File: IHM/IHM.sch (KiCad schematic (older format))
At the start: 29 parts, among them J1 JACK, SW1 BTN_R1, SW2 BTN_L1, SW3 BTN_L2, SW4 BTN_R2, U1 WeMos_D1_mini

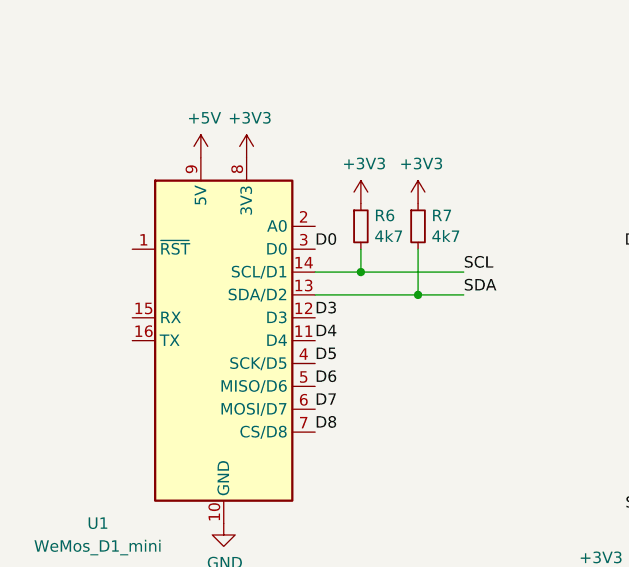
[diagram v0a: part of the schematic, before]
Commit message: Add LCSC references
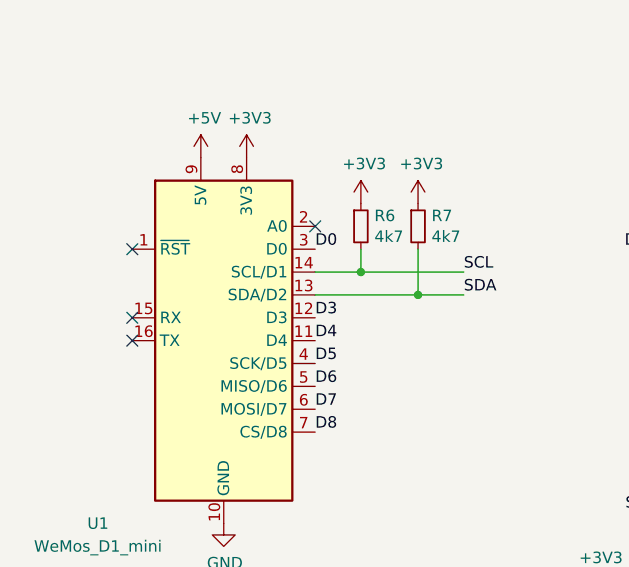
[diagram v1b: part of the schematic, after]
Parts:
- C1, C2, C3, C4, C5: LCSC (none) -> C14663
- R1, R2, R3, R4, R5: LCSC (none) -> C25804
- R6, R7: LCSC (none) -> C23162
- RG1, RR1: LCSC (none) -> C22843
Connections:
- no-connect marks 0 -> 4
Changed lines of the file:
@@
 F 2 "Resistor_SMD:R_0603_1608Metric" V 5280 3000 50  0001 C CNN
 F 3 "~" H 5350 3000 50  0001 C CNN
+F 4 "C25804" H 5350 3000 50  0001 C CNN "LCSC"
 	1    5350 3000
 	-1   0    0    1
@@
 F 2 "Resistor_SMD:R_0603_1608Metric" V 5230 1100 50  0001 C CNN
 F 3 "~" H 5300 1100 50  0001 C CNN
+F 4 "C22843" H 5300 1100 50  0001 C CNN "LCSC"
 	1    5300 1100
 	0    1    1    0
@@
 F 2 "Resistor_SMD:R_0603_1608Metric" V 5230 1600 50  0001 C CNN
 F 3 "~" H 5300 1600 50  0001 C CNN
+F 4 "C22843" H 5300 1600 50  0001 C CNN "LCSC"
 	1    5300 1600
 	0    1    1    0
@@
 F 2 "Resistor_SMD:R_0603_1608Metric" V 6230 3000 50  0001 C CNN
 F 3 "~" H 6300 3000 50  0001 C CNN
+F 4 "C25804" H 6300 3000 50  0001 C CNN "LCSC"
 	1    6300 3000
 	-1   0    0    1
@@
 F 2 "Resistor_SMD:R_0603_1608Metric" V 7180 3000 50  0001 C CNN
 F 3 "~" H 7250 3000 50  0001 C CNN
+F 4 "C25804" H 7250 3000 50  0001 C CNN "LCSC"
 	1    7250 3000
 	-1   0    0    1
@@
 F 2 "Resistor_SMD:R_0603_1608Metric" V 7330 1650 50  0001 C CNN
 F 3 "~" H 7400 1650 50  0001 C CNN
+F 4 "C25804" H 7400 1650 50  0001 C CNN "LCSC"
 	1    7400 1650
 	-1   0    0    1
@@
 F 2 "Resistor_SMD:R_0603_1608Metric" H 3900 3050 50  0001 C CNN
 F 3 "~" H 3900 3050 50  0001 C CNN
+F 4 "C23162" H 3900 3050 50  0001 C CNN "LCSC"
 	1    3900 3050
 	1    0    0    -1
@@
 F 2 "Resistor_SMD:R_0603_1608Metric" H 4150 3050 50  0001 C CNN
 F 3 "~" H 4150 3050 50  0001 C CNN
+F 4 "C23162" H 4150 3050 50  0001 C CNN "LCSC"
 	1    4150 3050
 	1    0    0    -1
@@
 F 2 "Capacitor_SMD:C_0603_1608Metric" H 5888 3200 50  0001 C CNN
 F 3 "~" H 5850 3350 50  0001 C CNN
+F 4 "C14663" H 5850 3350 50  0001 C CNN "LCSC"
 	1    5850 3350
 	1    0    0    -1
@@
 F 2 "Capacitor_SMD:C_0603_1608Metric" H 6838 3200 50  0001 C CNN
 F 3 "~" H 6800 3350 50  0001 C CNN
+F 4 "C14663" H 6800 3350 50  0001 C CNN "LCSC"
 	1    6800 3350
 	1    0    0    -1
@@
 F 2 "Capacitor_SMD:C_0603_1608Metric" H 7788 3200 50  0001 C CNN
 F 3 "~" H 7750 3350 50  0001 C CNN
+F 4 "C14663" H 7750 3350 50  0001 C CNN "LCSC"
 	1    7750 3350
 	1    0    0    -1
@@
 F 2 "Capacitor_SMD:C_0603_1608Metric" H 7038 1800 50  0001 C CNN
 F 3 "~" H 7000 1950 50  0001 C CNN
+F 4 "C14663" H 7000 1950 50  0001 C CNN "LCSC"
 	1    7000 1950
 	1    0    0    -1
@@
 F 2 "Capacitor_SMD:C_0603_1608Metric" H 8738 3200 50  0001 C CNN
 F 3 "~" H 8700 3350 50  0001 C CNN
+F 4 "C14663" H 8700 3350 50  0001 C CNN "LCSC"
 	1    8700 3350
 	1    0    0    -1
@@
 F 2 "Resistor_SMD:R_0603_1608Metric" V 8130 3000 50  0001 C CNN
 F 3 "~" H 8200 3000 50  0001 C CNN
+F 4 "C25804" H 8200 3000 50  0001 C CNN "LCSC"
 	1    8200 3000
 	-1   0    0    1
@@
 	1    0    0    -1
 $EndComp
+NoConn ~ 2900 3150
+NoConn ~ 2900 3450
+NoConn ~ 2900 3550
+NoConn ~ 3700 3050
 $EndSCHEMATC
